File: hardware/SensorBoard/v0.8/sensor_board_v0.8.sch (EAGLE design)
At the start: 48 parts, among them IC1 BMP280, J3 USB-MICROB, U1 ATMEGA328P, U10 CCS811, U11 RFM69HW, U2 TSL2561, U5 FT231XS, U7 SHT31, U8 MCP1703/3.3V, U9 MCP1703CB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

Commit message: Added traces for WAKE and INT pin
CCS811 requires WAKE pin to be triggered before every communication. INT
can be useful in the future for lower power or threshold alerts.
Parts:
- C5: value 0.1uF -> 1uF
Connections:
- new net INT: U1.PD7(AIN1), U10.INT
- new net N$6: U10.PWM, U10.SENSE
- new net WAKE: U1.PD4(XCK/T0), U10.WAKE

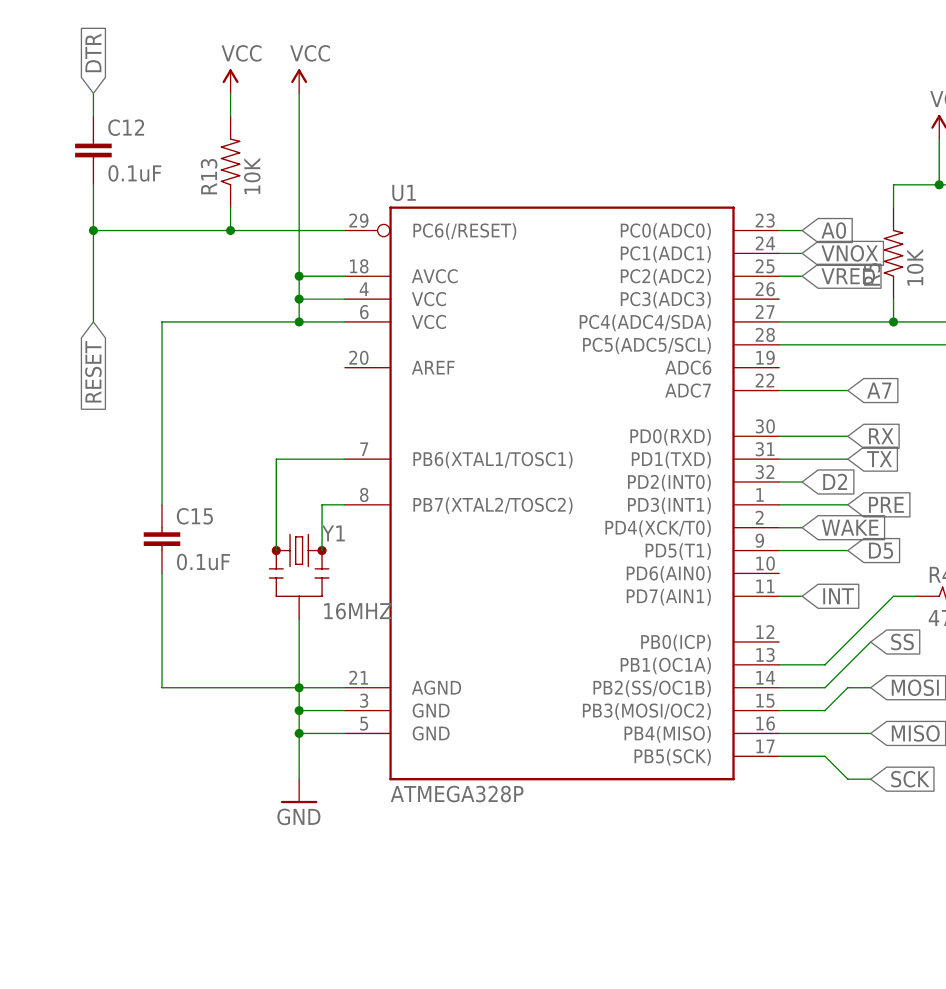
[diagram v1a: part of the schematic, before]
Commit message: Replaced ATmega328P TQFP with QFN/MLF Package
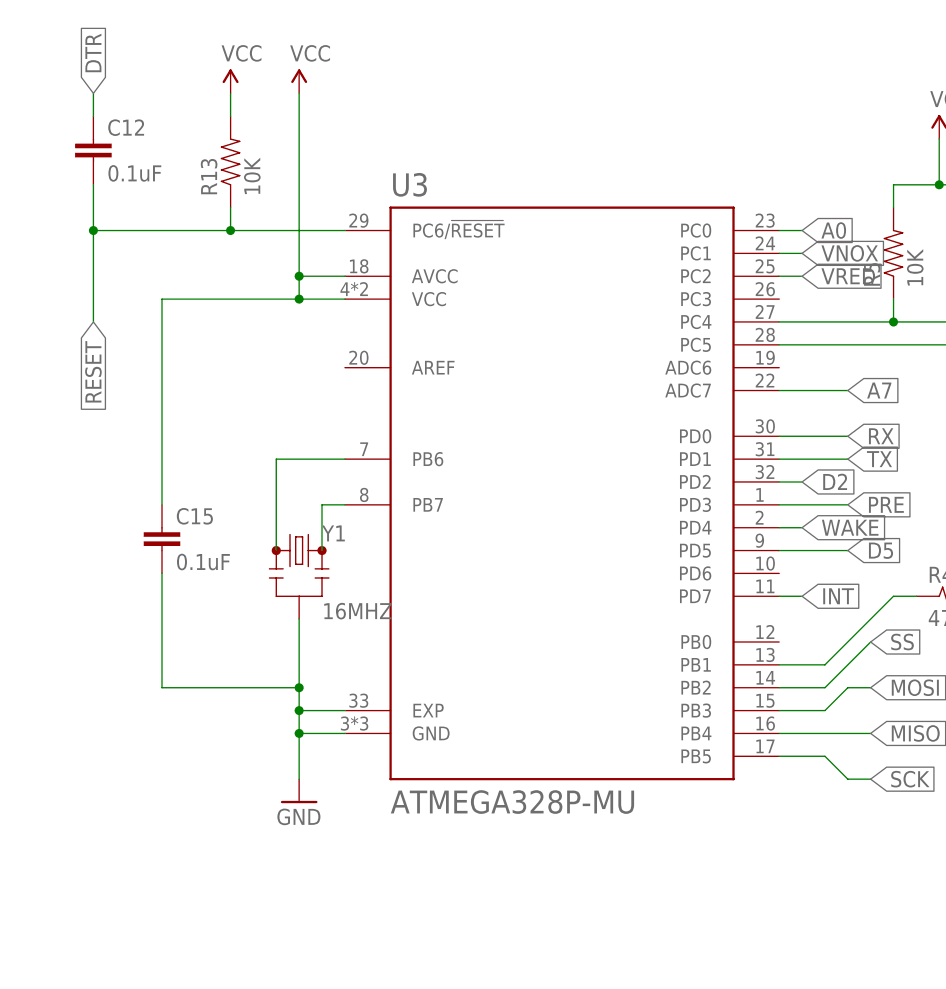
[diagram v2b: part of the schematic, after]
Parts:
- removed U1: ATMEGA328P, SparkFun-DigitalIC:ATMEGA328P_TQFP
- added U3: ATMEGA328P-MU, ATMEGA328P-MU:ATMEGA328P-MU
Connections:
- net A0: now also U3.PC0; no longer U1.PC0(ADC0)
- net A7: now also U3.ADC7; no longer U1.ADC7
- net D2: now also U3.PD2; no longer U1.PD2(INT0)
- net D5: now also U3.PD5; no longer U1.PD5(T1)
- net GND: now also U3.EXP, U3.GND; no longer U1.AGND, U1.GND@3, U1.GND@5
- net INT: now also U3.PD7; no longer U1.PD7(AIN1)
- net MISO: now also U3.PB4; no longer U1.PB4(MISO)
- net MOSI: now also U3.PB3; no longer U1.PB3(MOSI/OC2)
- net N$2: now also U3.PB1; no longer U1.PB1(OC1A)
- net N$4: now also U3.PB7; no longer U1.PB7(XTAL2/TOSC2)
- net N$5: now also U3.PB6; no longer U1.PB6(XTAL1/TOSC1)
- net PRE: now also U3.PD3; no longer U1.PD3(INT1)
- net RESET: now also U3.PC6/!RESET; no longer U1.PC6(/RESET)
- net RX: now also U3.PD0; no longer U1.PD0(RXD)
- net SCK: now also U3.PB5; no longer U1.PB5(SCK)
- net SCL: now also U3.PC5; no longer U1.PC5(ADC5/SCL)
- net SDA: now also U3.PC4; no longer U1.PC4(ADC4/SDA)
- net SS: now also U3.PB2; no longer U1.PB2(SS/OC1B)
- net TX: now also U3.PD1; no longer U1.PD1(TXD)
- net VCC: now also U3.AVCC, U3.VCC; no longer U1.AVCC, U1.VCC@4, U1.VCC@6
- net VNOX: now also U3.PC1; no longer U1.PC1(ADC1)
- net VRED: now also U3.PC2; no longer U1.PC2(ADC2)
- net WAKE: now also U3.PD4; no longer U1.PD4(XCK/T0)
